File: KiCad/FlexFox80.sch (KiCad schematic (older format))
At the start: 41 parts, among them J102 Jumper_NO_Small, J503 DET, J504 GND, J505 DET, J506 GND, J507 DET, J508 GND, P103 Phoenix, P502 Phoenix, Q101 LMN400E01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

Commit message: Schematic changes
Schematic
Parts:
- removed C502, C503, C504: np, Capacitors_SMD:C_0805_HandSoldering, symbol Device:C_Small
- removed J102: Jumper_NO_Small, Wire_Connections_Bridges:Solder-Jumper-NO-SMD-Pad_Small, symbol Device:Jumper_NO_Small
- removed J503, J505, J507: DET, Pin_Headers:Pin_Header_Straight_1x01_circle_pad, symbol FlexFox80-rescue:CONN_01X01-ARDF-2-Band-MiniTx-rescue
- removed J504, J506, J508: GND, Pin_Headers:Pin_Header_Straight_1x01, symbol FlexFox80-rescue:CONN_01X01-ARDF-2-Band-MiniTx-rescue
- removed P103: Phoenix, Sockets:Phoenix_3.81mm_3pos, symbol FlexFox80-rescue:CONN_01X03-ARDF-2-Band-MiniTx-rescue
- removed P502: Phoenix, Oddities:Dummy_Empty_3, symbol FlexFox80-rescue:CONN_01X03-ARDF-2-Band-MiniTx-rescue
- removed R502, R503, R504: 0, Resistors_SMD:Zero_Ohm_0805_HandSoldering, symbol Device:R
- added J101: DIN-5_180degree, symbol Connector:DIN-5_180degree
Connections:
- wire segments 87 -> 58
- no-connect marks 3 -> 4
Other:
- note removed: "2m RF Section"
- note removed: "Strain Relief Board #2"
- note removed: "Strain Relief Board #3"
- note removed: "Strain Relief Board #4"
- moved on the sheet: C117, C119, C120, C122, C123, C126, C128, C131, D301B, HS101, L106, L108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

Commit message: Updates to Schematic
Updates to Schematic
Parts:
- removed D301: D_Schottky_x2_KCom_Dual, TO_SOT_Packages_SMD:SOT-363_Handsolder, symbol FlexFox80-rescue:D_Schottky_x2_KCom_Dual-ARDF-2-Band-MiniTx-rescue
- added D?: Dual Schottky, TO_SOT_Packages_SMD:SOT-363-0.65, symbol Device:D_Schottky_ALT
- C117: footprint Capacitors_SMD:C_1210_HandSoldering -> Capacitors_SMD:C_1210; Description (none) -> CAP CER 22UF 25V X5R 1210; Manufacturer (none) -> Samsung Electro-Mechanics; Manufacturer PN (none) -> CL32A226MAJNNNE
- C119: Description (none) -> CAP TANT 47UF 10% 20V 2917; Manufacturer (none) -> KEMET; Manufacturer PN (none) -> T495D476K020ATE175
- C120, C122: footprint Capacitors_SMD:C_0805_HandSoldering -> Capacitors_SMD:C_0805; Description (none) -> CAP CER 0.47UF 100V X7R 0805; Manufacturer (none) -> AVX Corporation; Manufacturer PN (none) -> 08051C474K4Z2A
- C123, C131: footprint Capacitors_SMD:C_0805_HandSoldering -> Capacitors_SMD:C_0805; Description (none) -> CAP CER 1100PF 50V NP0 0805; Manufacturer (none) -> KEMET; Manufacturer PN (none) -> C0805C112J5GAC7800
- C126: footprint Capacitors_SMD:C_0805_HandSoldering -> Capacitors_SMD:C_0805; Description (none) -> CAP CER 1800PF 100V C0G 0805; Manufacturer (none) -> TDK Corporation; Manufacturer PN (none) -> CGA4F2C0G2A182J085AA
- C128: footprint Capacitors_SMD:C_0805_HandSoldering -> Capacitors_SMD:C_0805; Description (none) -> CAP CER 91PF 100V NP0 0805; Manufacturer (none) -> KEMET; Manufacturer PN (none) -> C0805C910J1GAC7800
- D102: Description (none) -> DIODE ZENER 4.7V 500MW SOD123; Manufacturer (none) -> Diodes Incorporated; Manufacturer PN (none) -> BZT52C4V7-13-F
- D104: footprint Diodes_SMD:SOD-323F_Handsolder -> Capacitors_SMD:C_0603; Description (none) -> VARISTOR 0603; Link <a href=\"https://www.digikey.com/product-detail/en/comchip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 -> <a href=\"https://www.digikey.com/products/en?keywords=CG06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; Manufacturer (none) -> Bourns Inc.; Manufacturer PN (none) -> CG0603MLC-05LE; Part No. 641-1219-1-ND -> CG0603MLC-05LECT-ND
- HS101, L104, L106, L108, Q102: Description (none) -> TH; Manufacturer (none) -> TH; Manufacturer PN (none) -> TH
- J101: Description (none) -> TH; Link (none) -> <a href=\"https://www.digikey.com/products/en?keywords=CP-7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; Manufacturer (none) -> TH; Manufacturer PN (none) -> TH; Part No. (none) -> CP-7050-ND
- Q101: value LMN400E01 -> LMN200B02; footprint TO_SOT_Packages_SMD:SOT-363_Handsolder -> TO_SOT_Packages_SMD:SOT-363-0.65; Description (none) -> MCU LOAD SWITCH 200MA SOT-363; Link <a href=\"https://www.digikey.com/products/en?keywords=LMN4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 -> <a href=\"https://www.digikey.com/products/en?keywords=LMN2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; Manufacturer (none) -> Diodes Incorporated; Manufacturer PN (none) -> LMN200B02-7; Part No. LMN400E01-7 -> LMN200B02DICT-ND
- U107: Description (none) -> IC GATE DRVR LOW-SIDE SOT23-6; Link <a href=\"https://www.digikey.com/products/en?keywords=296-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 -> <a href=\"https://www.digikey.com/products/en?keywords=LM51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; Manufacturer (none) -> Texas Instruments; Manufacturer PN (none) -> LM5134BMFX/NOPB; Part No. 296-40244-1-ND -> LM5134BMFX/NOPB-ND
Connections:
- wire segments 58 -> 59
- no-connect marks 4 -> 3

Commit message: Design Updates
Specifying components
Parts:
- C117: Digi-Key Part No. (none) -> 1276-3373-1-ND; Part No. 1276-3373-1-ND -> (none)
- C119: Digi-Key Part No. (none) -> 399-3904-1-ND; Link <a href=\"https://www.digikey.com/products/en?keywords=399-3885-1-ND\">Link</a> -> <a href=\"https://www.digikey.com/products/en?keywords=399-3904-1-ND\">Link</a>; Manufacturer PN T495D476K020ATE175 -> T495X476K020ATE150; Part No. 399-3885-1-ND -> (none)
- C120, C122: Digi-Key Part No. (none) -> 478-9924-1-ND; Part No. 478-9924-1-ND -> (none)
- C123: Digi-Key Part No. (none) -> 399-14552-1-ND; Part No. 399-14552-1-ND -> (none)
- C126: Digi-Key Part No. (none) -> 445-5752-1-ND; Part No. 445-5752-1-ND -> (none)
- C128: Digi-Key Part No. (none) -> 399-17459-1-ND; Part No. 399-17459-1-ND -> (none)
- D101: renamed from D?; Digi-Key Part No. (none) -> MBD54DWT1GOSCT-ND; Link (none) -> <a href=\"https://www.digikey.com/products/en?keywords=MBD5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
- D102: Digi-Key Part No. (none) -> BZT52C4V7-13FDICT-ND; Part No. BZT52C4V7-13FDICT-ND -> (none)
- D104: Digi-Key Part No. (none) -> CG0603MLC-05LECT-ND; Part No. CG0603MLC-05LECT-ND -> (none)
- HS101: Digi-Key Part No. (none) -> HS220-ND; Part No. HS220-ND -> (none)
- J101: Digi-Key Part No. (none) -> CP-7050-ND; Part No. CP-7050-ND -> (none)
- L104: Digi-Key Part No. (none) -> FT50A-43 (Amidon); Part No. Amidon FT50A-43 -> (none)
- L106, L108: Digi-Key Part No. (none) -> T60-2 (Amidon); Part No. T60-2 -> (none)
- Q101: Digi-Key Part No. (none) -> LMN200B02DICT-ND; Part No. LMN200B02DICT-ND -> (none)
- Q102: Digi-Key Part No. (none) -> IRF610PBF-ND; Part No. IRF610PBF-ND -> (none)
- U107: Digi-Key Part No. (none) -> LM5134BMFX/NOPB-ND; Part No. LM5134BMFX/NOPB-ND -> (none)
- W105, W106, W108, W111, W113, W117: Digi-Key Part No. (none) -> np; Part No. np -> (none)

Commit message: Design Updates
Defining parts and footprints
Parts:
- C131: Digi-Key Part No. (none) -> 399-14552-1-ND; Part No. 399-14552-1-ND -> (none)
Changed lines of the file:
@@
 $Comp
 L Device:C_Small C131
-U 1 1 607FCDED
+U 1 1 60A9B90E
 P 7500 3600
 F 0 "C131" H 7510 3670 50  0000 L CNN
@@
 F 2 "Capacitors_SMD:C_0805" H 7500 3600 50  0001 C CNN
 F 3 "" H 7500 3600 50  0000 C CNN
-F 4 "399-14552-1-ND" H 7500 3600 60  0001 C CNN "Part No."
+F 4 "399-14552-1-ND" H 7500 3600 50  0001 C CNN "Digi-Key Part No."
 F 5 "<a href=\"https://www.digikey.com/products/en?keywords=399-14552-1-ND\">Link</a>" H 7500 3600 60  0001 C CNN "Link"
 F 6 "KEMET" H 7500 3600 50  0001 C CNN "Manufacturer"

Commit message: Design Updates
Updating schematic parts
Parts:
- C119: footprint Capacitors_SMD:C_2917_7343_Metric_HandSoldering -> Capacitors_SMD:C_2917
- J101: footprint (none) -> Connect:SDF-50J
- U107: footprint TO_SOT_Packages_SMD:SOT-23-6_Handsolder -> TO_SOT_Packages_SMD:SOT-23-6-LM5134
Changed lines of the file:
@@
 F 0 "U107" H 3450 4350 61  0000 R CNB
 F 1 "LM5134B" H 3600 4250 61  0000 R CNB
-F 2 "TO_SOT_Packages_SMD:SOT-23-6_Handsolder" H 3300 3100 50  0001 L CNN
+F 2 "TO_SOT_Packages_SMD:SOT-23-6-LM5134" H 3300 3100 50  0001 L CNN
 F 3 "" H 3350 3650 50  0001 C CNN
 F 4 "LM5134BMFX/NOPB-ND" H 3150 3950 50  0001 C CNN "Digi-Key Part No."
@@
 F 0 "C119" V 4250 2650 50  0000 L CNN
 F 1 "47uF low ESR" V 4000 2350 50  0000 L CNN
-F 2 "Capacitors_SMD:C_2917_7343_Metric_HandSoldering" H 4150 2700 50  0001 C CNN
+F 2 "Capacitors_SMD:C_2917" H 4150 2700 50  0001 C CNN
 F 3 "" H 4150 2700 50  0001 C CNN
 F 4 "399-3904-1-ND" H 4150 2700 50  0001 C CNN "Digi-Key Part No."
@@
 F 0 "J101" H 8650 3250 50  0000 C CNN
 F 1 "DIN-5_180degree" H 8500 2634 50  0001 C CNN
-F 2 "" H 8500 3000 50  0001 C CNN
-F 3 "" H 8500 3000 50  0001 C CNN
+F 2 "Connect:SDF-50J" H 8500 3000 50  0001 C CNN
+F 3 "https://www.cuidevices.com/product/resource/sdf-j.pdf" H 8500 3000 50  0001 C CNN
 F 4 "CP-7050-ND" H 8500 3000 50  0001 C CNN "Digi-Key Part No."
 F 5 "<a href=\"https://www.digikey.com/products/en?keywords=CP-7050-ND\">Link</a>" H 8500 3000 50  0001 C CNN "Link"

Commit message: Design Updates
Updated schematics parts descriptions
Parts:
- D102: symbol FlexFox80-rescue:ZENER-ARDF-2-Band-MiniTx-rescue -> Diode:BZT52C4V7
- D104: symbol FlexFox80-rescue:TVS-ARDF-2-Band-MiniTx-rescue -> Power_Protection:TVS_Diode
- L104: symbol FlexFox80-rescue:INDUCTOR_CT-ARDF-2-Band-MiniTx-rescue -> Device:INDUCTOR_CT
- L106, L108: symbol FlexFox80-rescue:INDUCTOR_SMALL-ARDF-2-Band-MiniTx-rescue -> Device:INDUCTOR_SMALL
- Q101: symbol FlexFox80-rescue:LMN200B01-ARDF-2-Band-MiniTx-rescue -> Power_Protection:LMN200B01
- Q102: symbol FlexFox80-rescue:IRF610_TO220-ARDF-2-Band-MiniTx-rescue -> Transistor_FET:IRF610_TO220
- U107: symbol FlexFox80-rescue:LM5134-ARDF-2-Band-MiniTx-rescue -> Driver_FET:LM5134
- W105, W106, W108, W111, W113, W117: symbol FlexFox80-rescue:TEST_SCOPE-ARDF-2-Band-MiniTx-rescue -> special:TEST_SCOPE
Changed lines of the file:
@@
 $EndComp
 $Comp
-L FlexFox80-rescue:INDUCTOR_SMALL-ARDF-2-Band-MiniTx-rescue L106
+L Device:INDUCTOR_SMALL L106
 U 1 1 58A77A86
 P 6150 3400
@@
 Connection ~ 2650 3850
 $Comp
-L FlexFox80-rescue:LM5134-ARDF-2-Band-MiniTx-rescue U107
+L Driver_FET:LM5134 U107
 U 1 1 5AA8446F
 P 3150 3950
@@
 6th order Chebychev\n3.9MHz 3dB cut-off\nw/ node at 10.7MHz
 $Comp
-L FlexFox80-rescue:INDUCTOR_SMALL-ARDF-2-Band-MiniTx-rescue L108
+L Device:INDUCTOR_SMALL L108
 U 1 1 5C0D7F1D
 P 7150 3400
@@
 $EndComp
 $Comp
-L FlexFox80-rescue:TEST_SCOPE-ARDF-2-Band-MiniTx-rescue W105
+L special:TEST_SCOPE W105
 U 1 1 5C0EAA8C
 P 2650 3800
@@
 $EndComp
 $Comp
-L FlexFox80-rescue:TEST_SCOPE-ARDF-2-Band-MiniTx-rescue W108
+L special:TEST_SCOPE W108
 U 1 1 5C0EB478
 P 3950 4000
@@
 Connection ~ 3950 3850
 $Comp
-L FlexFox80-rescue:TEST_SCOPE-ARDF-2-Band-MiniTx-rescue W111
+L special:TEST_SCOPE W111
 U 1 1 5C0EDCBD
 P 5800 3250
@@
 $EndComp
 $Comp
-L FlexFox80-rescue:TEST_SCOPE-ARDF-2-Band-MiniTx-rescue W113
+L special:TEST_SCOPE W113
 U 1 1 5C0EE9E8
 P 6500 3250
@@
 $EndComp
 $Comp
-L FlexFox80-rescue:TEST_SCOPE-ARDF-2-Band-MiniTx-rescue W117
+L special:TEST_SCOPE W117
 U 1 1 5C0EEADD
 P 7700 3250
@@
 $EndComp
 $Comp
-L FlexFox80-rescue:TEST_SCOPE-ARDF-2-Band-MiniTx-rescue W106
+L special:TEST_SCOPE W106
 U 1 1 5C0F543D
 P 2750 3250
@@
 	6400 3400 6500 3400
 $Comp
-L FlexFox80-rescue:IRF610_TO220-ARDF-2-Band-MiniTx-rescue Q102
+L Transistor_FET:IRF610_TO220 Q102
 U 1 1 5C100056
 P 4600 3800
@@
 $EndComp
 $Comp
-L FlexFox80-rescue:LMN200B01-ARDF-2-Band-MiniTx-rescue Q101
+L Power_Protection:LMN200B01 Q101
 U 1 1 5C64951A
 P 3250 2500
@@
 	2750 3250 3150 3250
 $Comp
-L FlexFox80-rescue:ZENER-ARDF-2-Band-MiniTx-rescue D102
+L Diode:BZT52C4V7 D102
 U 1 1 5C71D9FE
 P 3150 2950
@@
 $EndComp
 $Comp
-L FlexFox80-rescue:TVS-ARDF-2-Band-MiniTx-rescue D104
+L Power_Protection:TVS_Diode D104
 U 1 1 5CB36EAB
 P 8650 2350
@@
 $EndComp
 $Comp
-L FlexFox80-rescue:INDUCTOR_CT-ARDF-2-Band-MiniTx-rescue L104
+L Device:INDUCTOR_CT L104
 U 1 1 5CB66258
 P 4700 3400

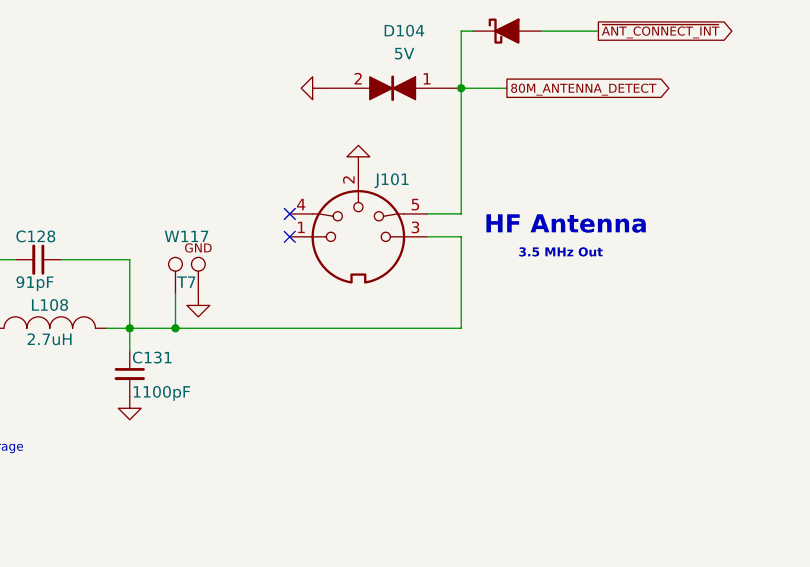
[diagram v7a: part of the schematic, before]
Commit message: PCB Updates
o Started PCB layout
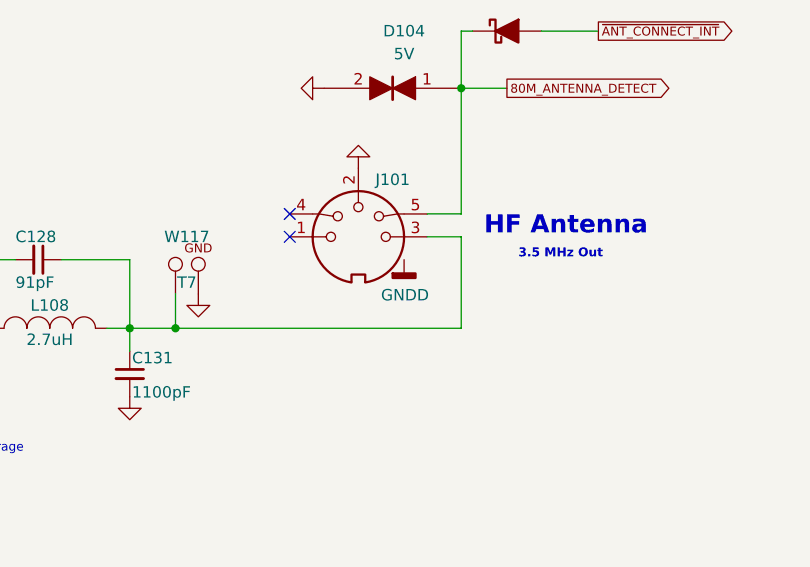
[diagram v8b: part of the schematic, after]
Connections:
- net GNDD: now reaches J101.E
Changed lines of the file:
@@
+	1    0    0    -1
+$EndComp
+$Comp
+L power:GNDD #PWR0215
+U 1 1 60E20F36
+P 8700 3100
+F 0 "#PWR0215" H 8700 2850 50  0001 C CNN
+F 1 "GNDD" H 8704 2945 50  0000 C CNN
+F 2 "" H 8700 3100 50  0001 C CNN
+F 3 "" H 8700 3100 50  0001 C CNN
+	1    8700 3100
 	1    0    0    -1
 $EndComp
